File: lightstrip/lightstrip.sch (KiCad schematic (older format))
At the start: 19 parts, among them J1 Connector

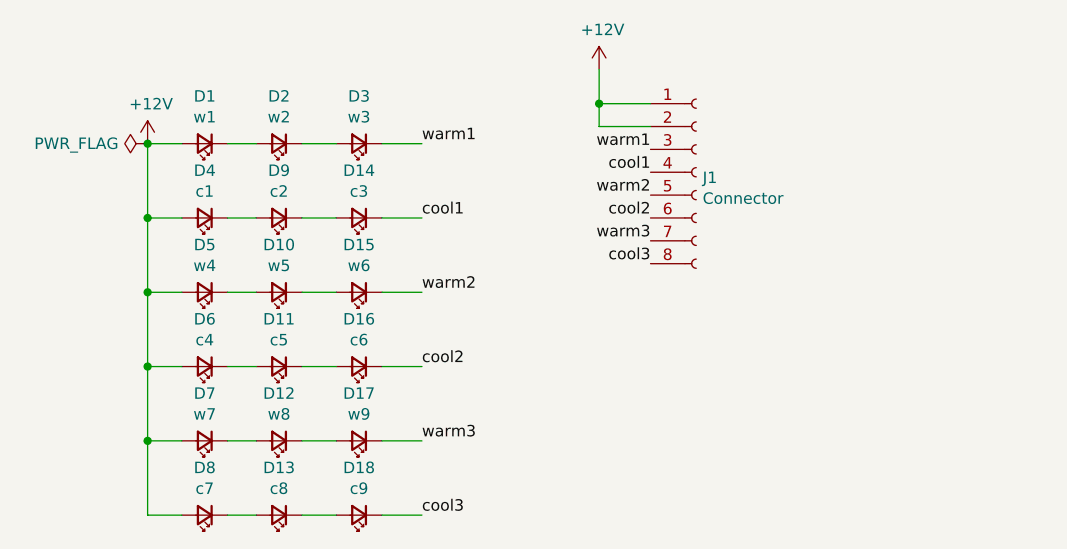
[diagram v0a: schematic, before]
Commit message: Spread strip to 9".
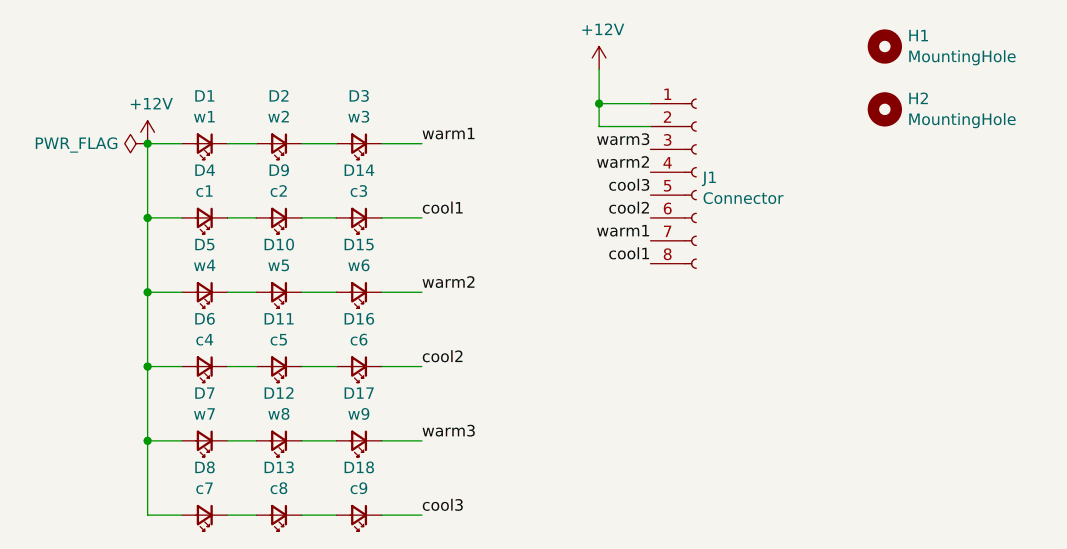
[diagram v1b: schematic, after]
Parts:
- added H1, H2: MountingHole, MountingHole:MountingHole_2.2mm_M2, symbol Mechanical:MountingHole
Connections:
- net cool1: now also J1.8 (Pin_8); no longer J1.4 (Pin_4)
- net cool3: now also J1.5 (Pin_5); no longer J1.8 (Pin_8)
- net warm1: now also J1.7 (Pin_7); no longer J1.3 (Pin_3)
- net warm2: now also J1.4 (Pin_4); no longer J1.5 (Pin_5)
- net warm3: now also J1.3 (Pin_3); no longer J1.7 (Pin_7)
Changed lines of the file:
@@
 	1    0    0    -1
 $EndComp
-Text Label 4575 1500 2    50   ~ 0
+Text Label 4575 1900 2    50   ~ 0
 warm1
-Text Label 4575 1600 2    50   ~ 0
+Text Label 4575 2000 2    50   ~ 0
 cool1
 Wire Wire Line
@@
 Text Label 3575 1475 0    50   ~ 0
 warm1
-Text Label 4575 1700 2    50   ~ 0
+Text Label 4575 1600 2    50   ~ 0
 warm2
 Text Label 4575 1800 2    50   ~ 0
 cool2
-Text Label 4575 1900 2    50   ~ 0
+Text Label 4575 1500 2    50   ~ 0
 warm3
-Text Label 4575 2000 2    50   ~ 0
+Text Label 4575 1700 2    50   ~ 0
 cool3
 $Comp
@@
 	4350 1400 4350 1300
 Connection ~ 4350 1300
+$Comp
+L Mechanical:MountingHole H1
+U 1 1 60600B87
+P 5600 1050
+F 0 "H1" H 5700 1096 50  0000 L CNN
+F 1 "MountingHole" H 5700 1005 50  0000 L CNN
+F 2 "MountingHole:MountingHole_2.2mm_M2" H 5600 1050 50  0001 C CNN
+F 3 "~" H 5600 1050 50  0001 C CNN
+	1    5600 1050
+	1    0    0    -1
+$EndComp
+$Comp
+L Mechanical:MountingHole H2
+U 1 1 6060219C
+P 5600 1325
+F 0 "H2" H 5700 1371 50  0000 L CNN
+F 1 "MountingHole" H 5700 1280 50  0000 L CNN
+F 2 "MountingHole:MountingHole_2.2mm_M2" H 5600 1325 50  0001 C CNN
+F 3 "~" H 5600 1325 50  0001 C CNN
+	1    5600 1325
+	1    0    0    -1
+$EndComp
 $EndSCHEMATC
